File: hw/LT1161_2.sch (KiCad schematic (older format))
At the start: 8 parts, among them U901 MOSFET_DRIVER_LT1161, U902 MOSFET_IPG20N04S4L11ATMA1, U903 MOSFET_IPG20N04S4L11ATMA1, U904 MOSFET_IPG20N04S4L11ATMA1, U905 MOSFET_IPG20N04S4L11ATMA1

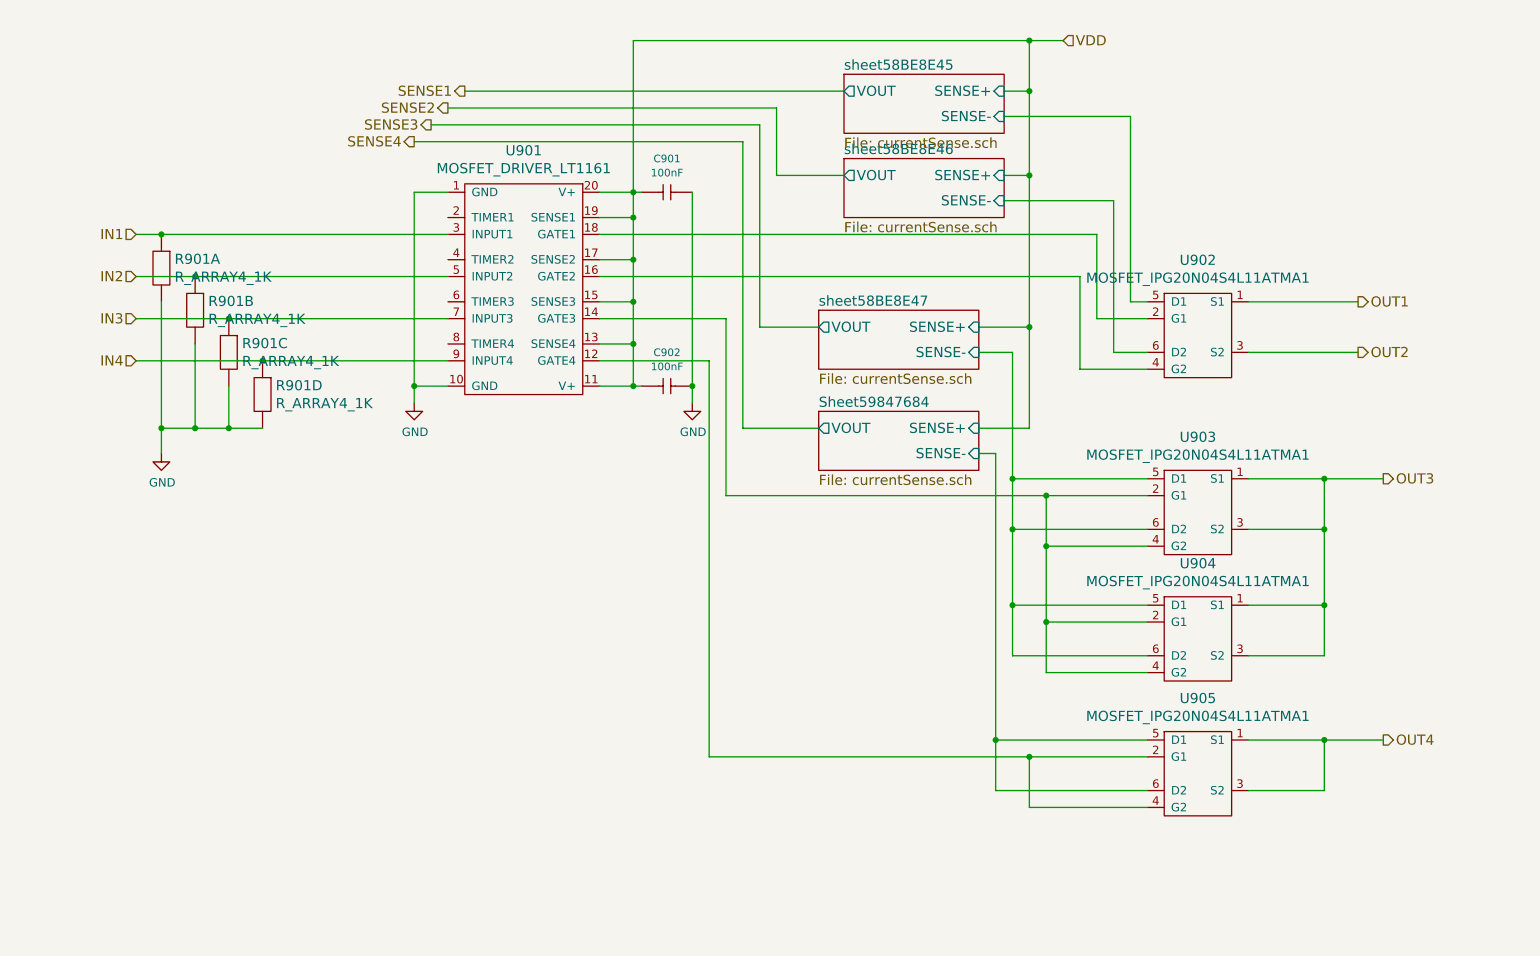
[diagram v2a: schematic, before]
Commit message: at least shortcirucuit protection works
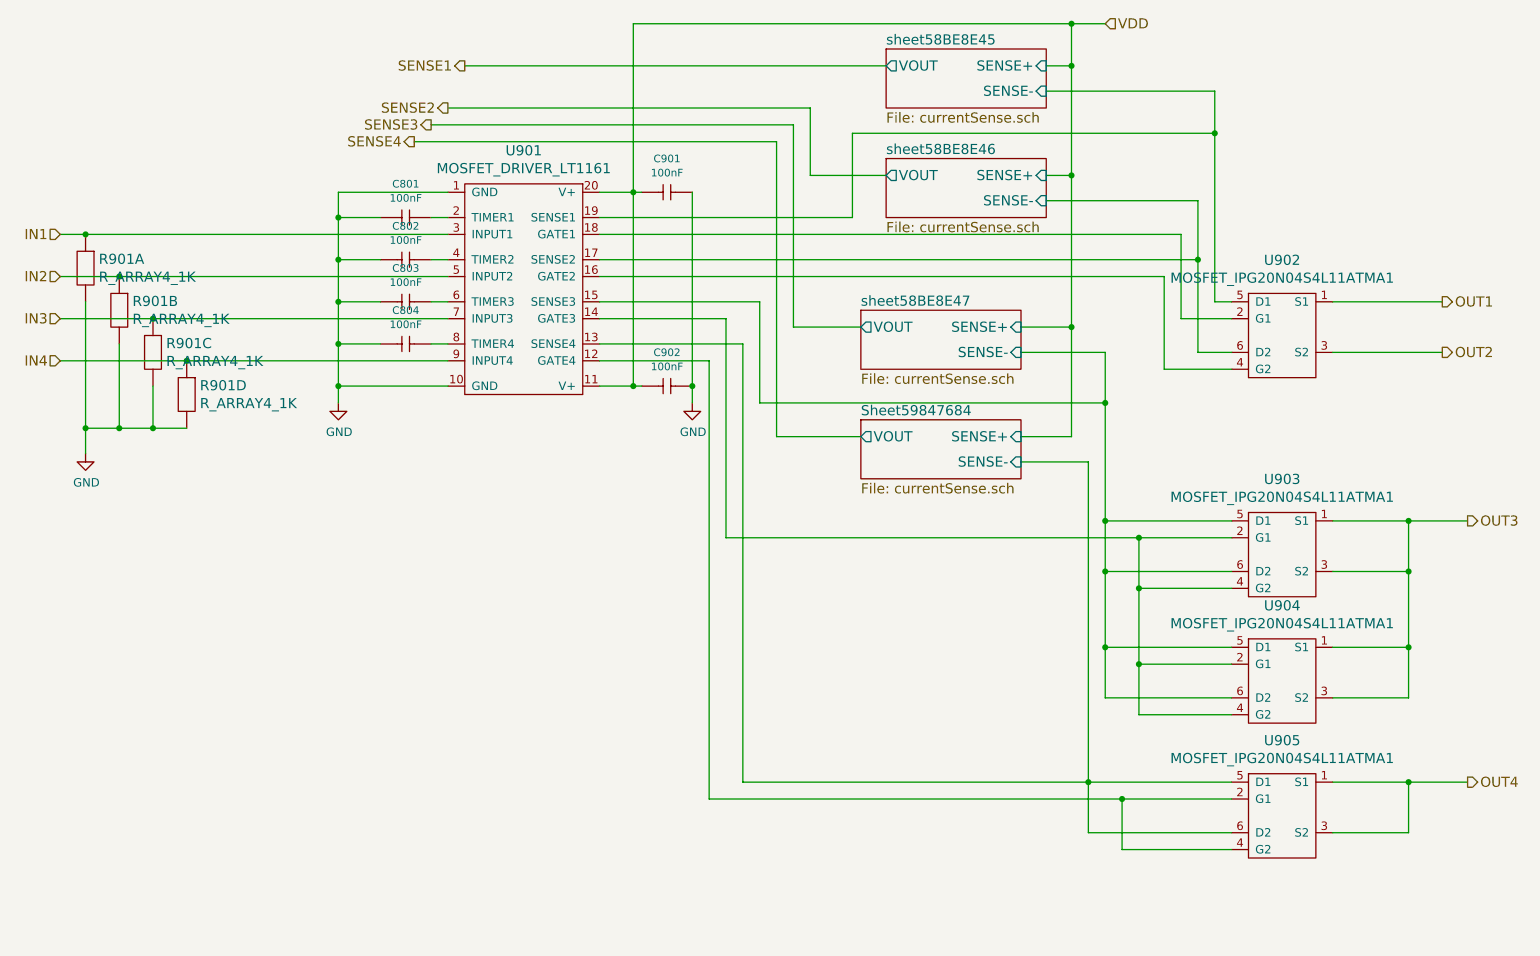
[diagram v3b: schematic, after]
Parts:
- added C801, C802, C803, C804: 100nF, kemet:0603, symbol 100nF
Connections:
- net GND: now also C801.1 (C1), C802.1 (C1), C803.1 (C1), C804.1 (C1)
- net Sheet59847684/SENSE-: now also U901.13 (SENSE4)
- net VDD: no longer U901.13 (SENSE4), U901.15 (SENSE3), U901.17 (SENSE2), U901.19 (SENSE1)
- net sheet58BE8E45/SENSE-: now also U901.19 (SENSE1)
- net sheet58BE8E46/SENSE-: now also U901.17 (SENSE2)
- net sheet58BE8E47/SENSE-: now also U901.15 (SENSE3)
- net at U901.2 (TIMER1): now also C801.2 (C2)
- net at U901.4 (TIMER2): now also C802.2 (C2)
- net at U901.6 (TIMER3): now also C803.2 (C2)
- net at U901.8 (TIMER4): now also C804.2 (C2)
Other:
- moved on the sheet: R901A, R901B, R901C, R901D, U902, U903, U904, U905

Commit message: starting to draw version 4.0.0
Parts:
- renumbered C901 to C805, C902 to C806, R901 to R801, U901 to U801, U902 to U802, U903 to U803, U904 to U804, U905 to U805
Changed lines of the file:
@@
 $EndComp
 $Comp
-L MOSFET_DRIVER_LT1161 U901
+L MOSFET_DRIVER_LT1161 U801
 U 1 1 58BE8E74
 P 4200 2300
-F 0 "U901" H 4200 3097 60  0000 C CNN
+F 0 "U801" H 4200 3097 60  0000 C CNN
 F 1 "MOSFET_DRIVER_LT1161" H 4200 2991 60  0000 C CNN
 F 2 "usevolt:SO20" H 4250 3175 60  0001 C CNN
@@
 AR Path="/58C7B0A8/595CED52" Ref="C?"  Part="1"
 AR Path="/59542AAB/595CED52" Ref="C?"  Part="1"
-AR Path="/5954FB0E/595CED52" Ref="C901"  Part="1"
-F 0 "C901" H 5050 1949 45  0000 C CNN
+AR Path="/5954FB0E/595CED52" Ref="C805"  Part="1"
+F 0 "C805" H 5050 1949 45  0000 C CNN
 F 1 "100nF" H 5050 1865 45  0000 C CNN
 F 2 "kemet:0603" H 5030 1900 20  0001 C CNN
@@
 AR Path="/58C7B0A8/595CED53" Ref="C?"  Part="1"
 AR Path="/59542AAB/595CED53" Ref="C?"  Part="1"
-AR Path="/5954FB0E/595CED53" Ref="C902"  Part="1"
-F 0 "C902" H 5050 3099 45  0000 C CNN
+AR Path="/5954FB0E/595CED53" Ref="C806"  Part="1"
+F 0 "C806" H 5050 3099 45  0000 C CNN
 F 1 "100nF" H 5050 3015 45  0000 C CNN
 F 2 "kemet:0603" H 5030 3050 20  0001 C CNN
@@
 VDD
 $Comp
-L MOSFET_IPG20N04S4L11ATMA1 U902
+L MOSFET_IPG20N04S4L11ATMA1 U802
 U 1 1 595CED56
 P 8700 2600
-F 0 "U902" H 8700 3047 60  0000 C CNN
+F 0 "U802" H 8700 3047 60  0000 C CNN
 F 1 "MOSFET_IPG20N04S4L11ATMA1" H 8700 2941 60  0000 C CNN
 F 2 "usevolt:PG-TDSON-8-4" H 8700 3100 60  0001 C CNN
@@
 $EndComp
 $Comp
-L R_ARRAY4_1K R901
+L R_ARRAY4_1K R801
 U 1 1 595CED57
 P 1600 2200
-F 0 "R901" V 1547 2278 60  0000 L CNN
+F 0 "R801" V 1547 2278 60  0000 L CNN
 F 1 "R_ARRAY4_1K" V 1653 2278 60  0000 L CNN
 F 2 "usevolt:0603_array4" H 1500 2300 60  0001 C CNN
@@
 $EndComp
 $Comp
-L R_ARRAY4_1K R901
+L R_ARRAY4_1K R801
 U 2 1 595CED58
 P 1800 2450
-F 0 "R901" V 1747 2528 60  0000 L CNN
+F 0 "R801" V 1747 2528 60  0000 L CNN
 F 1 "R_ARRAY4_1K" V 1853 2528 60  0000 L CNN
 F 2 "usevolt:0603_array4" H 1700 2550 60  0001 C CNN
@@
 $EndComp
 $Comp
-L R_ARRAY4_1K R901
+L R_ARRAY4_1K R801
 U 3 1 595CED59
 P 2000 2700
-F 0 "R901" V 1947 2778 60  0000 L CNN
+F 0 "R801" V 1947 2778 60  0000 L CNN
 F 1 "R_ARRAY4_1K" V 2053 2778 60  0000 L CNN
 F 2 "usevolt:0603_array4" H 1900 2800 60  0001 C CNN
@@
 U 59847685
 F0 "Sheet59847684" 60
-F1 "currentSense.sch" 60
+F1 "currentSense3.sch" 60
 F2 "SENSE+" I R 7150 3200 60
 F3 "SENSE-" I R 7150 3350 60
@@
 SENSE4
 $Comp
-L MOSFET_IPG20N04S4L11ATMA1 U904
+L MOSFET_IPG20N04S4L11ATMA1 U804
 U 1 1 5955DCC6
 P 8700 4650
-F 0 "U904" H 8700 5097 60  0000 C CNN
+F 0 "U804" H 8700 5097 60  0000 C CNN
 F 1 "MOSFET_IPG20N04S4L11ATMA1" H 8700 4991 60  0000 C CNN
 F 2 "usevolt:PG-TDSON-8-4" H 8700 5150 60  0001 C CNN
@@
 $EndComp
 $Comp
-L MOSFET_IPG20N04S4L11ATMA1 U903
+L MOSFET_IPG20N04S4L11ATMA1 U803
 U 1 1 591C1D78
 P 8700 3900
-F 0 "U903" H 8700 4347 60  0000 C CNN
+F 0 "U803" H 8700 4347 60  0000 C CNN
 F 1 "MOSFET_IPG20N04S4L11ATMA1" H 8700 4241 60  0000 C CNN
 F 2 "usevolt:PG-TDSON-8-4" H 8700 4400 60  0001 C CNN
@@
 OUT3
 $Comp
-L MOSFET_IPG20N04S4L11ATMA1 U905
+L MOSFET_IPG20N04S4L11ATMA1 U805
 U 1 1 59847F80
 P 8700 5450
-F 0 "U905" H 8700 5897 60  0000 C CNN
+F 0 "U805" H 8700 5897 60  0000 C CNN
 F 1 "MOSFET_IPG20N04S4L11ATMA1" H 8700 5791 60  0000 C CNN
 F 2 "usevolt:PG-TDSON-8-4" H 8700 5950 60  0001 C CNN
@@
 OUT4
 $Comp
-L R_ARRAY4_1K R901
+L R_ARRAY4_1K R801
 U 4 1 5984A4D9
 P 2200 2950
-F 0 "R901" V 2147 3028 60  0000 L CNN
+F 0 "R801" V 2147 3028 60  0000 L CNN
 F 1 "R_ARRAY4_1K" V 2253 3028 60  0000 L CNN
 F 2 "usevolt:0603_array4" H 2100 3050 60  0001 C CNN
